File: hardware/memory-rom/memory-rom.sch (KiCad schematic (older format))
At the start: 27 parts, among them J1 Conn_Mem_Ext, J2 Conn_Power, U1 SST39VF040-70-4C-NHE, U2 74LVC1G86, U3 74LVC1G32, U4 74LVC1G332, U5 74LVC1G86, U6 MIC5504-3.3YM5

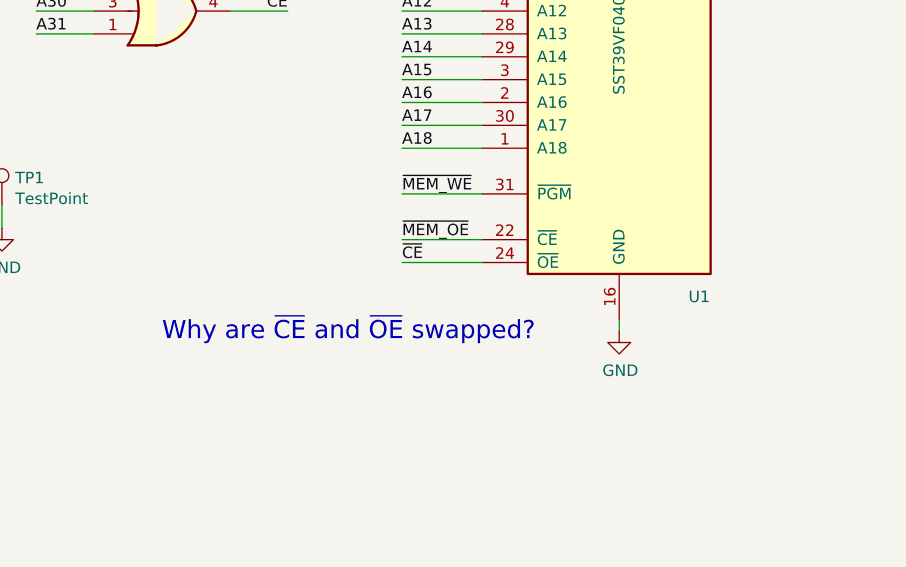
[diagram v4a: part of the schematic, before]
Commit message: Rev B of memory-rom: switch OE and CE
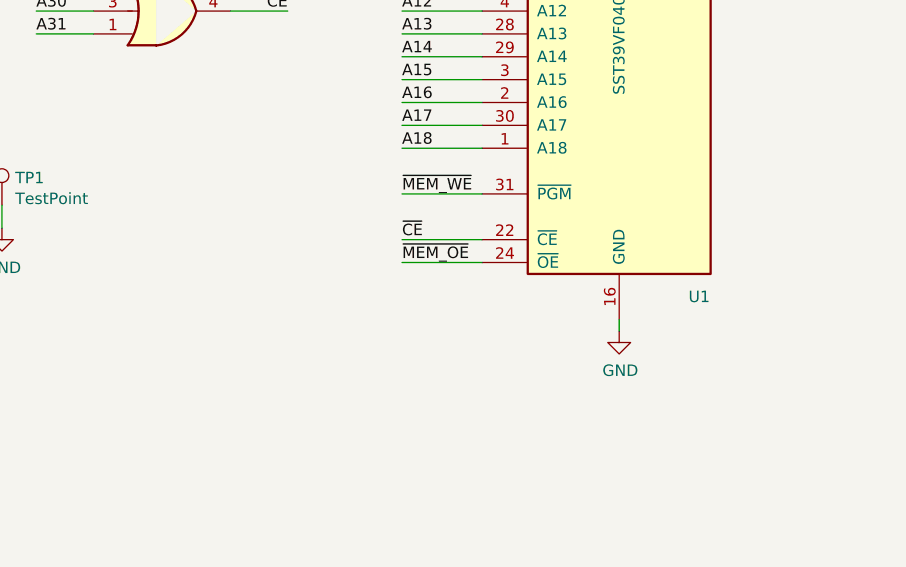
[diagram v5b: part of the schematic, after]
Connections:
- net ~CE: now also U1.22 (~CE); no longer U1.24 (~OE)
- net ~MEM_OE: now also U1.24 (~OE); no longer U1.22 (~CE)
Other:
- note removed: "Why are ~CE~ and ~OE~ swapped?"
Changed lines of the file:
@@
 Wire Wire Line
 	8000 4000 8000 4050
-Text Label 7050 3650 0    50   ~ 0
+Text Label 7050 3750 0    50   ~ 0
 ~MEM_OE
 Text Label 7050 3450 0    50   ~ 0
@@
 	7050 3450 7400 3450
 Wire Wire Line
-	7400 3650 7050 3650
+	7400 3750 7050 3750
 Wire Wire Line
 	1950 5800 1450 5800
@@
 	1    0    0    -1
 $EndComp
-Text Label 7050 3750 0    50   ~ 0
+Text Label 7050 3650 0    50   ~ 0
 ~CE
 Wire Wire Line
-	7050 3750 7400 3750
+	7050 3650 7400 3650
 Wire Wire Line
 	1450 6200 1600 6200
@@
 Wire Wire Line
 	5300 3500 5300 3600
-Text Notes 6000 4100 0    79   ~ 0
-Why are ~CE~ and ~OE~ swapped?
 $EndSCHEMATC
